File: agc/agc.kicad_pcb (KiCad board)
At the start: 2 copper layers, 72.4 x 59.1 mm, 63 parts, among them J5 SIL10, K1 TR, K10 HVMON, K11 HVMON, K2 TR, K3 VIN, K4 VOUT_TR, K5 TR, K6 TR, K7 HVMON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

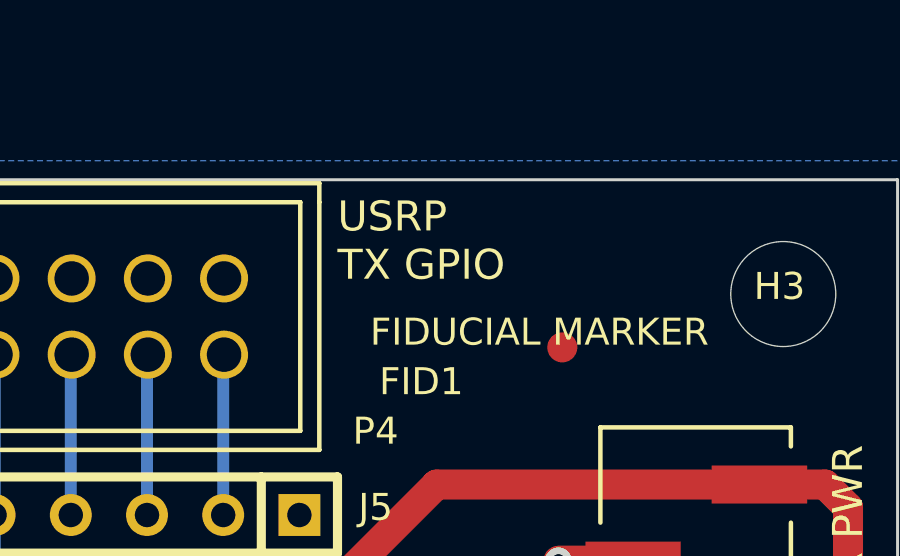
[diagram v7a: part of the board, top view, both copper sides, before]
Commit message: added digikey bom for control
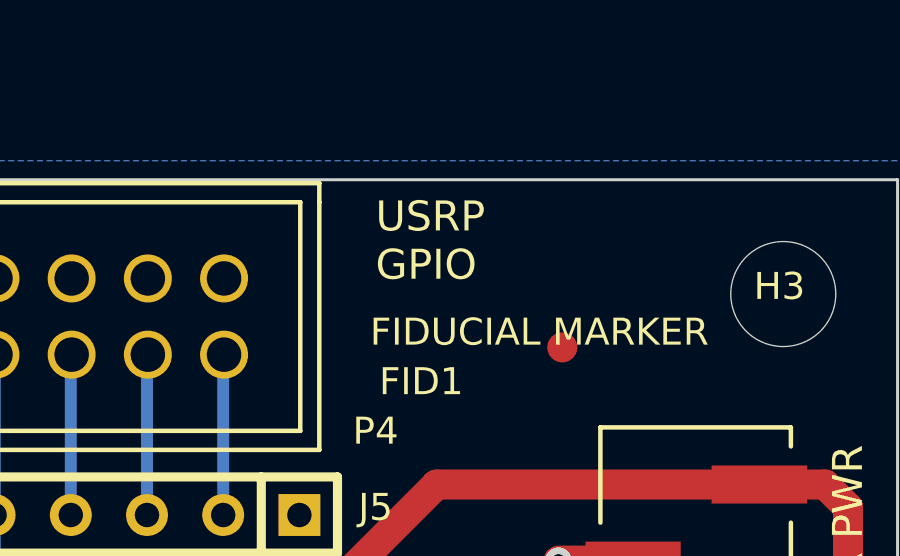
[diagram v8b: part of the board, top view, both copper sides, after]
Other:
- board text added: "USRP GPIO"
- board text removed: "USRP TX GPIO"
